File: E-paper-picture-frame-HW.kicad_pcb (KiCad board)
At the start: 4 copper layers, 170.2 x 111.2 mm, 106 parts, among them J1 Connector, USB-TYPE-C-16P, J2 Conn_01x02, Q1 AO3401A, Q2 BSS138, Q3 AO3401A, Q4 AO3401A, SW1 SS-2235-H2.0, U1 TPS63001DRCR, U2 TP4054, U3 ESP32-C6-MINI-1

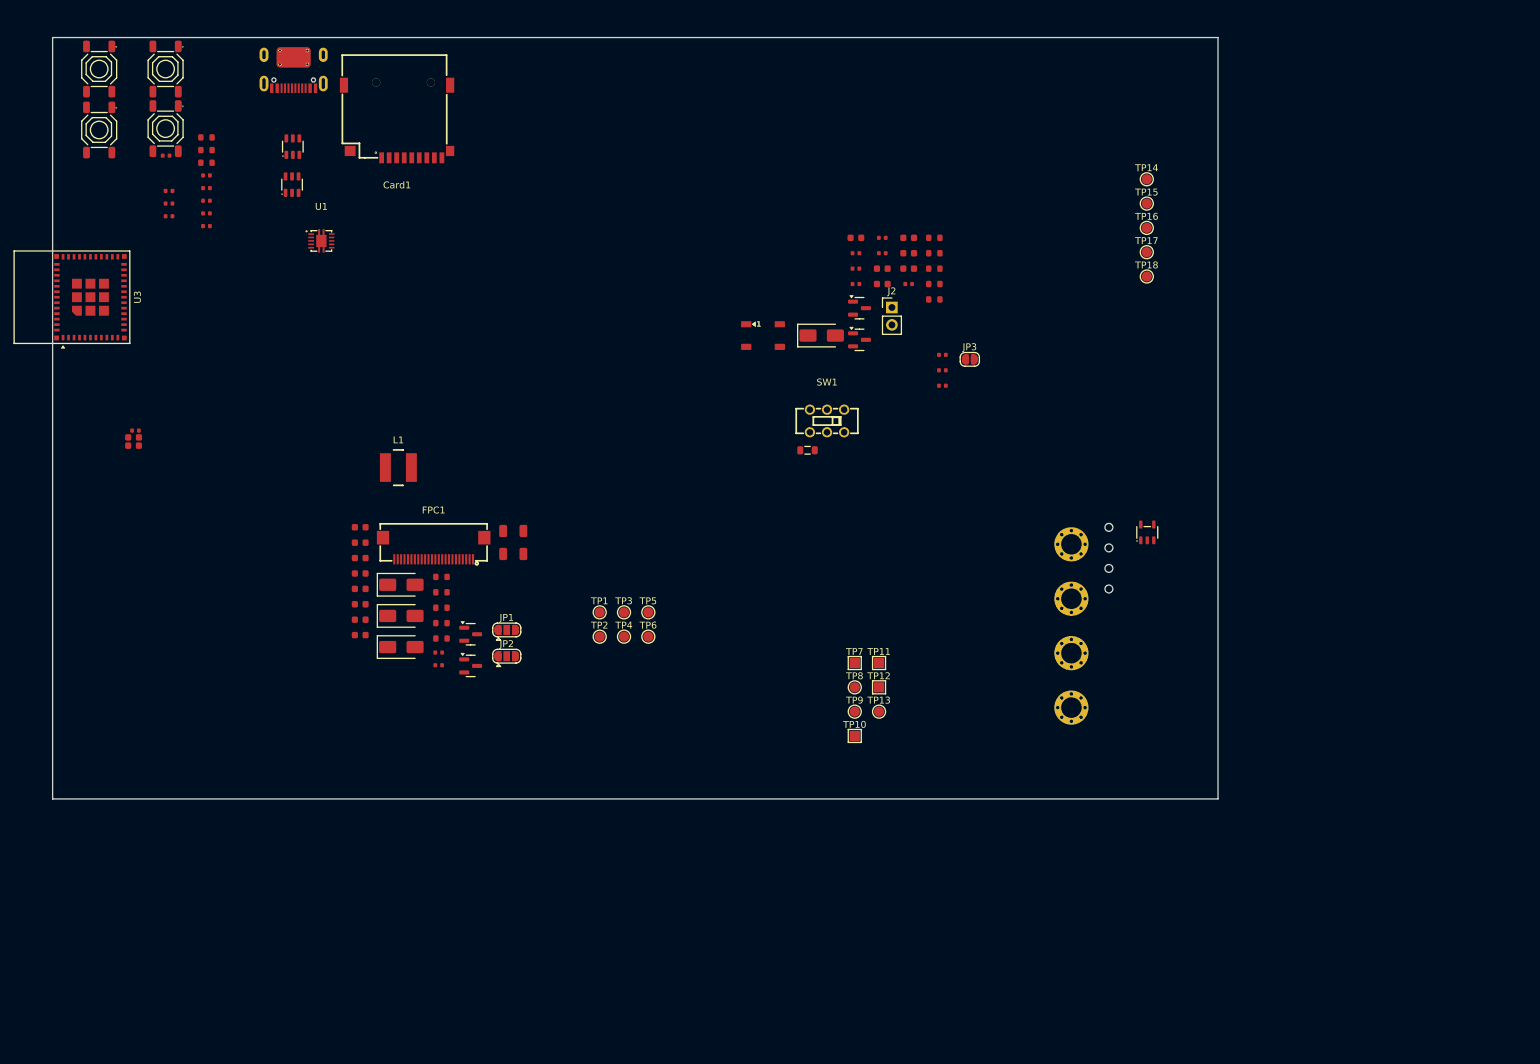
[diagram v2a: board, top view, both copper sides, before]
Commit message: Changed some parts for more common ones
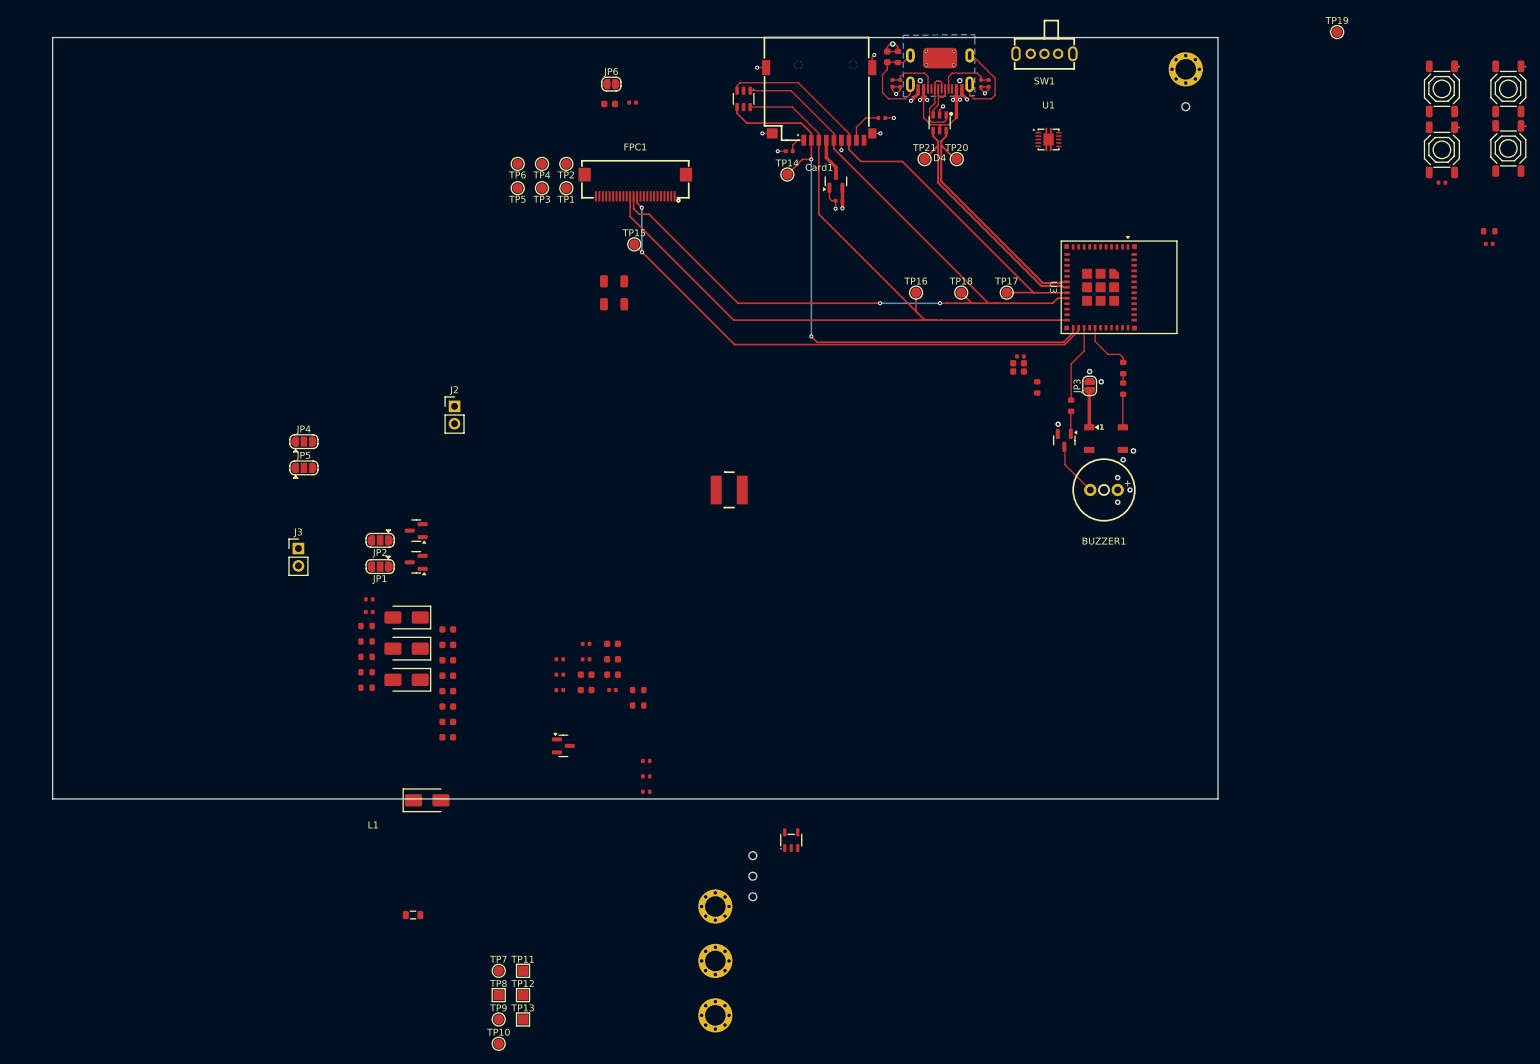
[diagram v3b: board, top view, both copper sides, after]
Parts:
- added BUZZER1: YS-MBZ9042C03R16, Libraries:BUZ-TH_BD9.0-P4.00-D0.6-FD, F.Cu at (176.4, 85.6)
- added C27: 10uF, PCM_JLCPCB:C_0603, F.Cu at (104.2, 29.2)
- added J3: Conn_01x02, Connector_PinHeader_2.54mm:PinHeader_1x02_P2.54mm_Vertical, F.Cu at (58.8, 94.1)
- added JP4: SolderJumper_3_Open, Jumper:SolderJumper-3_P1.3mm_Open_RoundedPad1.0x1.5mm, F.Cu at (59.6, 78.5)
- added JP5: SolderJumper_3_Open, Jumper:SolderJumper-3_P1.3mm_Open_RoundedPad1.0x1.5mm, F.Cu at (59.6, 82.3)
- added JP6: SolderJumper_2_Open, Jumper:SolderJumper-2_P1.3mm_Open_RoundedPad1.0x1.5mm, F.Cu at (104.5, 26.3)
- added Q5: AO3401A, PCM_JLCPCB:Q_SOT-23, F.Cu at (137.3, 40.5)
- added R27: 10kΩ, PCM_JLCPCB:R_0402, F.Cu at (107.6, 29.0)
- added TP19: TestPoint_EN, TestPoint:TestPoint_Pad_D1.5mm, F.Cu at (210.5, 18.7)
- added TP20: TestPoint_EN, TestPoint:TestPoint_Pad_D1.5mm, F.Cu at (154.9, 37.2)
- added TP21: TestPoint_EN, TestPoint:TestPoint_Pad_D1.5mm, F.Cu at (150.2, 37.2)
- D4: value SRV05-4_C7420376 -> USBLC6-2SC6; footprint PCM_JLCPCB:SOT-23-6_L2.9-W1.6-P0.95-LS2.8-BL-1 -> Libraries:SOT-23-6_L2.9-W1.6-P0.95-LS2.8-BL
- Q3: value AO3401A -> AO3400A
- R10, R16, R9: value 10Ω -> 100Ω
- R11: value 10Ω -> 10kΩ; footprint PCM_JLCPCB:R_0603 -> PCM_JLCPCB:R_0402
- R15: value 10kΩ -> 100Ω; footprint PCM_JLCPCB:R_0402 -> PCM_JLCPCB:R_0603
- SW1: value SS-2235-H2.0 -> SK12D07VG4; footprint Libraries:SW-TH_6P-L9.0-W3.6-P2.50_SS-2235-H2.0 -> Libraries:SW-TH_SK12D07VG4
- TP10: value TestPoint_3V3 -> TestPoint_VINA; footprint TestPoint:TestPoint_Pad_1.5x1.5mm -> TestPoint:TestPoint_Pad_D1.5mm
- TP11: value TestPoint_VDD -> TestPoint_3V3
- TP13: value TestPoint_CHRG -> TestPoint_VDD; footprint TestPoint:TestPoint_Pad_D1.5mm -> TestPoint:TestPoint_Pad_1.5x1.5mm
- TP7: value TestPoint_LIPO -> TestPoint_CHRG; footprint TestPoint:TestPoint_Pad_1.5x1.5mm -> TestPoint:TestPoint_Pad_D1.5mm
- TP8: value TestPoint_GND -> TestPoint_LIPO; footprint TestPoint:TestPoint_Pad_D1.5mm -> TestPoint:TestPoint_Pad_1.5x1.5mm
- TP9: value TestPoint_VINA -> TestPoint_GND
- moved S1 196.1 mm to (225.8, 27.0)
- moved S3 196.1 mm to (225.8, 35.9)
- moved S2 196.1 mm to (235.5, 27.0)
- moved S4 196.1 mm to (235.5, 35.7)
- moved R15 187.4 mm to (232.7, 47.8)
- moved R19 187.4 mm to (232.7, 49.6)
- moved C23 186.4 mm to (225.8, 40.7), turned to 180 degrees
- moved U3 147.5 mm to (175.9, 56.0), turned to -90 degrees
- moved R10 138.3 mm to (179.2, 70.8), turned to -90 degrees
- moved R9 138.1 mm to (179.2, 67.8), turned to -90 degrees
- moved C24 129.7 mm to (164.0, 68.3)
- moved C25 129.7 mm to (164.0, 67.1)
- moved C26 129.7 mm to (164.2, 66.1)
- moved R13 115.2 mm to (159.6, 26.2), turned to -90 degrees
- moved R14 114.4 mm to (158.5, 26.2), turned to -90 degrees
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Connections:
- net /MCU/GPIO9 renamed /MCU/Boot
- net Net-(J1-SHIELD) renamed /IO/USB_SHIELD
- C13 pad 1: Net-(JP3-A) -> /IO/LED_VDD
- C13 pad 2: Net-(D5-VDD) -> /IO/LED_VDD
- Card1 pad 7: /IO/SPI.MISO -> /Display/SPI.MISO
- D4 pad 1: /IO/USB D- -> /IO/USB_Dp
- D4 pad 3: /IO/USB D+ -> /IO/USB_Dn
- D4 pad 4: unconnected-(D4-I/O-Pad4) -> /MCU/USB D-
- D4 pad 6: unconnected-(D4-I/O-Pad6) -> /MCU/USB D+
- D5 pad 1: Net-(D5-VDD) -> /IO/LED_VDD
- D5 pad 4: Net-(D5-DIN) -> /IO/DIN
- D7 pad 3: /Display/SPI.MOSI -> /Display/SPI.MISO
- D7 pad 6: /IO/SPI.MISO -> /Display/SPI.MOSI
- J1 pad A6: /IO/USB D+ -> /IO/USB_Dp
- J1 pad A7: /IO/USB D- -> /IO/USB_Dn
- J1 pad B6: /IO/USB D+ -> /IO/USB_Dp
- J1 pad B7: /IO/USB D- -> /IO/USB_Dn
- JP3 pad 1: Net-(JP3-A) -> /IO/LED_VDD
- JP3 pad 2: /IO/VDD(SD) -> /IO/5V_USB
- Q3 pad 1: /IO/5V_USB -> Net-(Q3-G)
- Q3 pad 2: /IO/BAT+ -> GNDD
- Q3 pad 3: /IO/VDD_EXT_OPEN -> Net-(Q3-D)
- Q4 pad 1: /IO/SD3V3_EN -> /IO/5V_USB
- Q4 pad 2: +3.3V -> /IO/BAT+
- Q4 pad 3: /IO/VDD(SD) -> /IO/VDD_EXT_OPEN
- R10 pad 2: Net-(R10-Pad2) -> /IO/DIN
- R11 pad 1: Net-(R10-Pad2) -> /IO/USBCC2
- R11 pad 2: Net-(D5-DIN) -> GNDD
- R13 pad 1: /IO/USBCC2 -> /IO/USBCC1
- R15 pad 1: /IO/USBCC1 -> /IO/VDD_EXT
- R15 pad 2: GNDD -> /IO/EN
- R16 pad 1: /IO/VDD_EXT -> Net-(Q3-G)
- R16 pad 2: /IO/EN -> /IO/BUZZER_CTRL
- R9 pad 1: /IO/LED_IN -> /IO/LED_DIN
- SW1 pad 1: unconnected-(SW1-Pad1) -> /IO/VDD_EXT
- SW1 pad 2: unconnected-(SW1-Pad2) -> /IO/VDD_EXT_OPEN
- SW1 pad 3: /IO/VDD_EXT -> unconnected-(SW1-Pad3)
- SW1 pad 4: unconnected-(SW1-Pad4) -> GNDD
- SW1 pad 5: /IO/VDD_EXT_OPEN -> GNDD
- TP10 pad 1: +3.3V -> /IO/EN
- TP11 pad 1: /IO/VDD_EXT -> +3.3V
- TP12 pad 1: /IO/VDD_EXT_OPEN -> /IO/VDD_EXT
- TP13 pad 1: /IO/CHRG -> /IO/VDD_EXT_OPEN
- TP17 pad 1: /MCU/SPI2.MISO -> /Display/SPI.MISO
- TP7 pad 1: /IO/BAT+ -> /IO/CHRG
- TP8 pad 1: GNDD -> /IO/BAT+
- TP9 pad 1: /IO/EN -> GNDD
- U1 pad 1: unconnected-(U1-VOUT-Pad1) -> +3.3V
- U3 pad 10: /MCU/SPI2.MISO -> /IO/PS/SYNC
- U3 pad 12: /Display/EPD CS -> /MCU/GPIO0
- U3 pad 13: /IO/USER0 -> /MCU/GPIO1
- U3 pad 15: /Display/SPI.SCK -> /MCU/GPIO6
- U3 pad 17: /IO/USB D+ -> /MCU/USB D+
- U3 pad 18: /IO/USB D- -> /MCU/USB D-
- U3 pad 19: /Display/EPD3V3_EN -> /Display/SPI.MISO
- U3 pad 20: /IO/SD3V3_EN -> /Display/SPI.SCK
- U3 pad 24: /MCU/GPIO18 -> /Display/SPI.MOSI
- U3 pad 26: /MCU/GPIO20 -> /Display/EPD CS
- U3 pad 27: /MCU/GPIO21 -> /IO/BUZZER_CTRL
- U3 pad 29: /MCU/GPIO23 -> /IO/LED_DIN
- U3 pad 30: /MCU/GPIO18(RTX) -> /MCU/GPIO16
- U3 pad 31: /MCU/GPIO17(RX) -> /MCU/GPIO17
- U3 pad 9: /Display/SPI.MOSI -> /IO/USER0
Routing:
- net /Display/SPI.SCK: track 0.00 -> 123.2 mm, vias 0 -> 2
- net /Display/SPI.MOSI: track 0.00 -> 122.8 mm
- net /IO/CS: track 0.00 -> 87.2 mm, vias 0 -> 2
- net /Display/EPD CS: track 0.00 -> 80.1 mm, vias 0 -> 2
- net /Display/SPI.MISO: track 0.00 -> 68.2 mm
- net /MCU/USB D-: track 0.00 -> 35.8 mm
- net /MCU/USB D+: track 0.00 -> 35.1 mm
- net /IO/USB_SHIELD: track 0.00 -> 28.2 mm
- net GNDD: track 0.00 -> 24.8 mm, vias 0 -> 12
- net /IO/5V_USB: track 0.00 -> 18.4 mm, vias 0 -> 4
- net /IO/USB_Dp: track 0.00 -> 11.5 mm
- net /IO/BUZZER_CTRL: track 0.00 -> 11.4 mm
- net /IO/USBCC1: track 0.00 -> 8.52 mm
- net /IO/USBCC2: track 0.00 -> 7.91 mm
- net /IO/LED_DIN: track 0.00 -> 7.77 mm
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- added copper zone on B.Cu, net /IO/USB_SHIELD
- added copper zone on In1.Cu, net GNDD

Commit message: Finished USB, SD card and Power Mmt layout
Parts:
- moved TP9 162.1 mm to (190.1, 37.0)
- moved TP12 158.9 mm to (175.7, 24.6)
- moved TP8 157.4 mm to (187.1, 37.0)
- moved TP13 156.9 mm to (160.2, 21.8)
- moved TP10 156.9 mm to (177.3, 37.5)
- moved L2 155.8 mm to (175.7, 28.3), turned to 180 degrees
- moved TP11 154.9 mm to (179.1, 28.0)
- moved C16 152.0 mm to (248.8, 75.6)
- moved R18 152.0 mm to (256.4, 80.1)
- moved TP7 135.9 mm to (162.1, 41.8)
- moved D6 133.7 mm to (163.5, 28.4), turned to -90 degrees
- moved Q4 117.4 mm to (167.8, 28.9), turned to 90 degrees
- moved J2 110.3 mm to (187.1, 41.2), turned to 90 degrees
- moved C18 109.4 mm to (172.4, 32.0), turned to -90 degrees
- moved C20 108.8 mm to (179.5, 31.3)
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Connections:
- net Net-(JP6-A) renamed /IO/PROG
- Card1 pad 7: /Display/SPI.MISO -> /IO/SPI.MISO
- D7 pad 3: /Display/SPI.MISO -> /IO/SPI.MISO
- TP17 pad 1: /Display/SPI.MISO -> /MCU/SPI2.MISO
- U3 pad 19: /Display/SPI.MISO -> /MCU/SPI2.MISO
- U3 pad 24: /Display/SPI.MOSI -> /MCU/GPIO18
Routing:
- net /Display/SPI.MOSI: track 122.8 -> 12.6 mm
- net /Display/SPI.SCK: track 123.2 -> 15.8 mm, vias 2 -> 0
- net /Display/EPD CS: track 80.1 -> 0.00 mm, vias 2 -> 0
- net /IO/CS: track 87.2 -> 14.2 mm, vias 2 -> 0
- net /Display/SPI.MISO: track 68.2 -> 0.00 mm
- net /IO/BAT+: track 0.00 -> 39.1 mm
- net GNDD: track 24.8 -> 52.7 mm, vias 12 -> 34
- net /MCU/USB D-: track 35.8 -> 10.7 mm
- net /MCU/USB D+: track 35.1 -> 10.5 mm
- net /IO/VDD_EXT: track 0.00 -> 23.9 mm
- net /IO/SPI.MISO: track 0.00 -> 22.4 mm
- net /IO/VDD_EXT_OPEN: track 0.00 -> 18.1 mm
- net /IO/EN: track 0.00 -> 14.2 mm
- net /IO/5V_USB: track 18.4 -> 32.3 mm, vias 4 -> 3
- net +3.3V: track 5.36 -> 15.8 mm, vias 3 -> 4
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- added copper zone on F.Cu, net GNDD
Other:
- board text added: "100mA->200mA"
